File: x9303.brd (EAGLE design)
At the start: 133 x 59 mm, 158 parts, among them CN11 ERC12864-2, CN12 SD-CARD_10P, IC1 7805DT, IC2 L1117, IC3 Pololu, IC4 MCP1700T30, J3 ERASE, K1 TP-1, K2 TP-1, K3 TP-1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

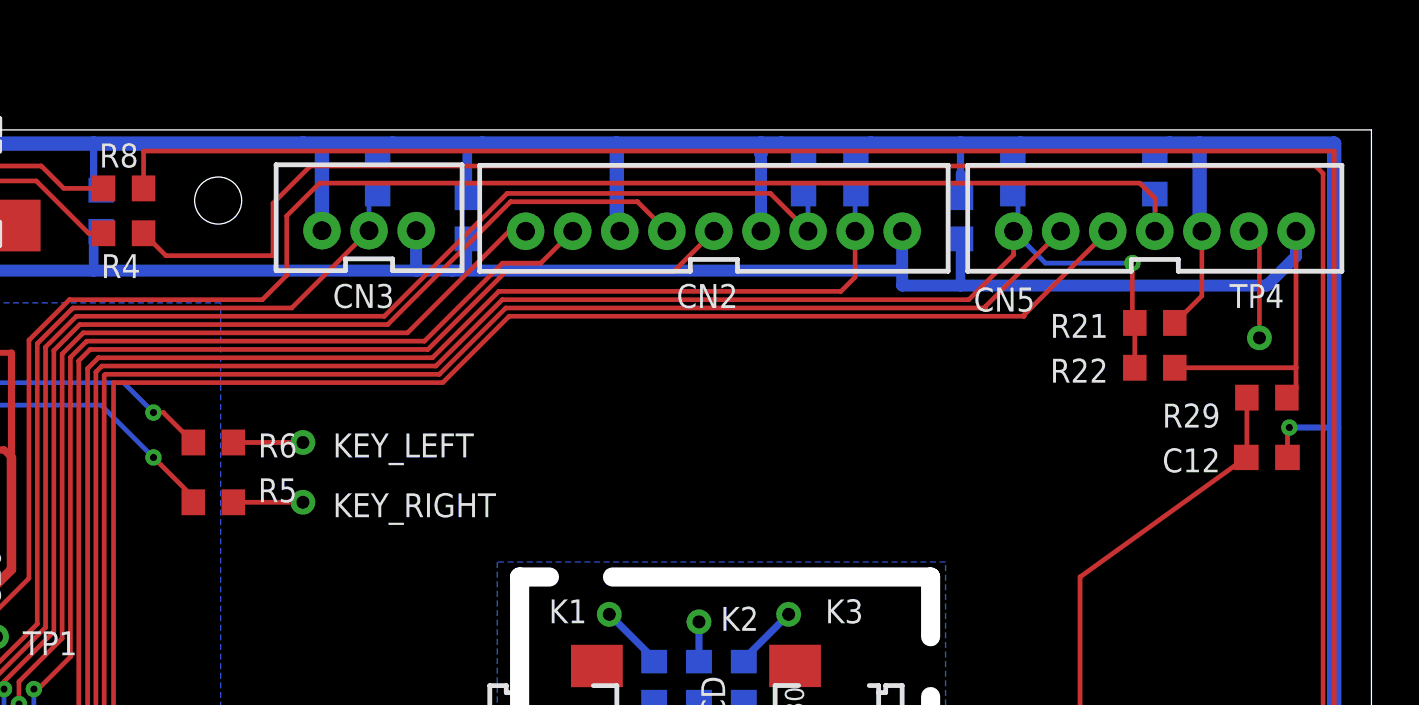
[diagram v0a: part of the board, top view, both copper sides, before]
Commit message: 
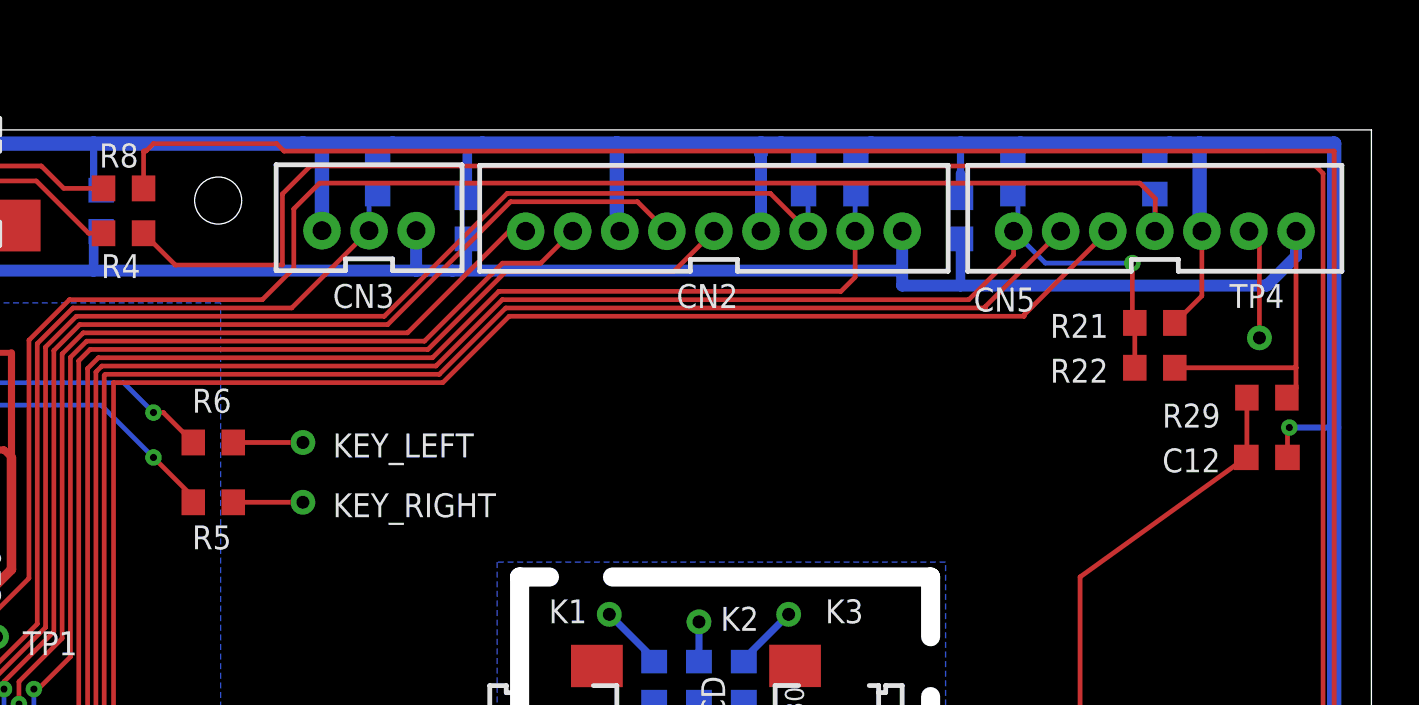
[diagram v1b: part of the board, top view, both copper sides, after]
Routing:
- net KEY-DOWN: track 84.0 -> 84.8 mm
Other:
- board text added: "CHARGER+"
- board text added: "TRN1"
- board text added: "TRN2"
- board text added: "TRN3"
- board text removed: "Chargder+"

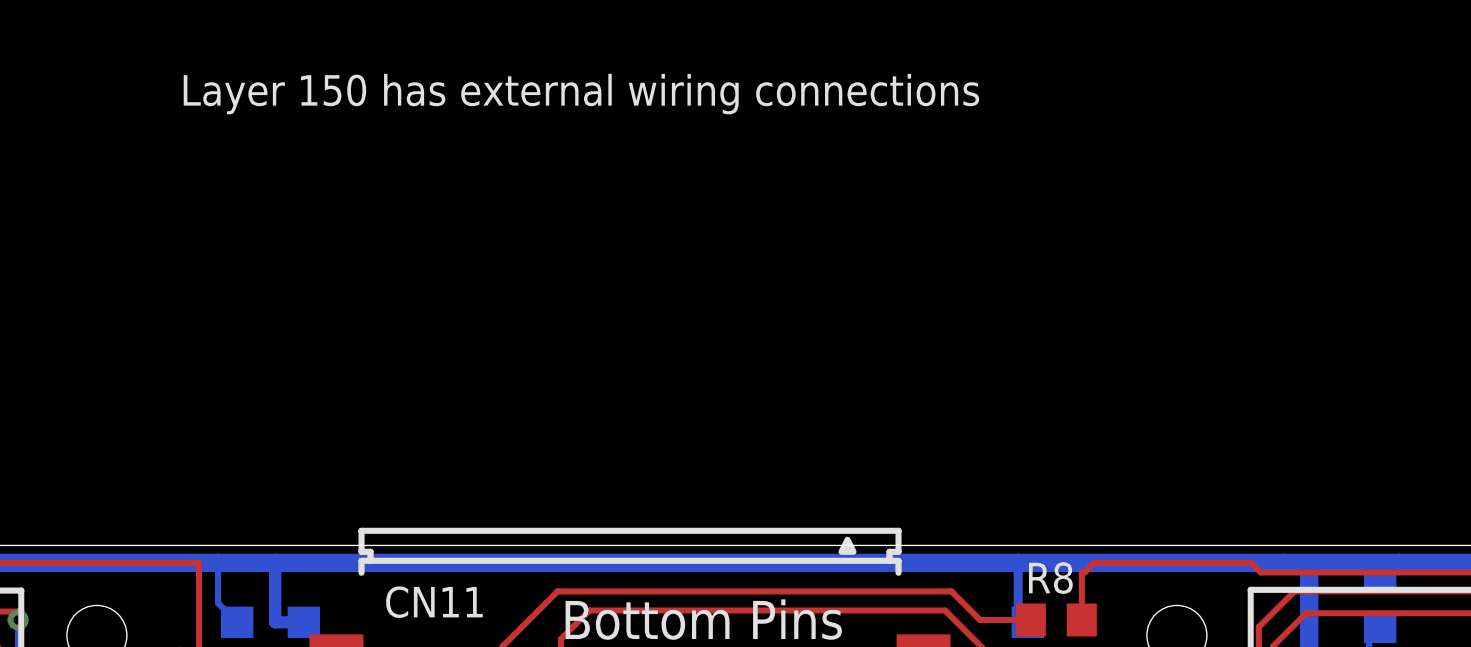
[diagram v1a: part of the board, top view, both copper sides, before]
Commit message: added pictures and docs added firmware binary added old JR9303 wiring and pin-out doc added lcd display adapter patch boards for different displays
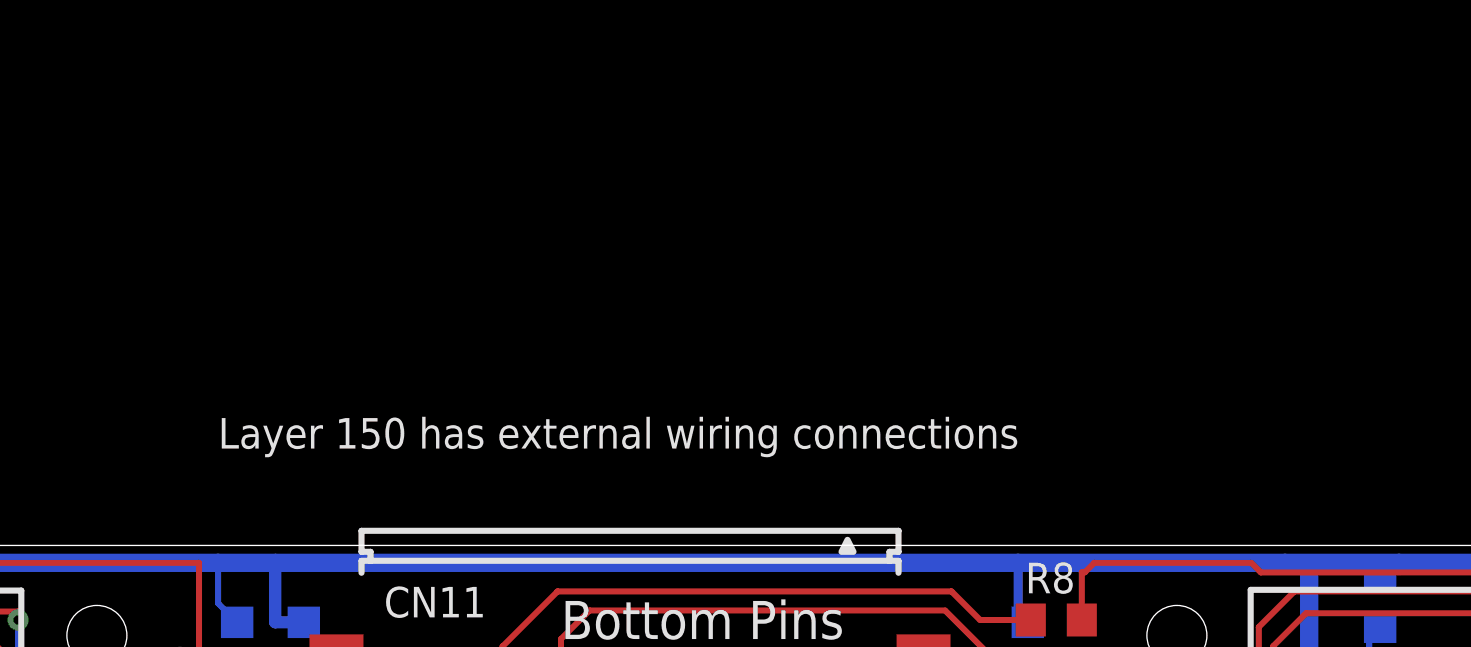
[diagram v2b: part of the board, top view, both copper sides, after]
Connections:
- net PWR_SW_BAT renamed PWR_SW_CTR_A&B
- net RF_MODULE_PWR renamed PWRSW_ON_A
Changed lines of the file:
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@@
 <layer number="14" name="Route14" color="22" fill="1" visible="no" active="no"/>
 <layer number="15" name="Route15" color="23" fill="1" visible="no" active="no"/>
-<layer number="16" name="Bottom" color="1" fill="1" visible="no" active="yes"/>
+<layer number="16" name="Bottom" color="1" fill="1" visible="yes" active="yes"/>
 <layer number="17" name="Pads" color="2" fill="1" visible="yes" active="yes"/>
 <layer number="18" name="Vias" color="2" fill="1" visible="yes" active="yes"/>
@@
 <layer number="20" name="Dimension" color="24" fill="1" visible="yes" active="yes"/>
 <layer number="21" name="tPlace" color="7" fill="1" visible="yes" active="yes"/>
-<layer number="22" name="bPlace" color="7" fill="1" visible="no" active="yes"/>
+<layer number="22" name="bPlace" color="7" fill="1" visible="yes" active="yes"/>
 <layer number="23" name="tOrigins" color="15" fill="1" visible="yes" active="yes"/>
-<layer number="24" name="bOrigins" color="15" fill="1" visible="no" active="yes"/>
+<layer number="24" name="bOrigins" color="15" fill="1" visible="yes" active="yes"/>
 <layer number="25" name="tNames" color="7" fill="1" visible="yes" active="yes"/>
-<layer number="26" name="bNames" color="7" fill="1" visible="no" active="yes"/>
+<layer number="26" name="bNames" color="7" fill="1" visible="yes" active="yes"/>
 <layer number="27" name="tValues" color="7" fill="1" visible="no" active="yes"/>
 <layer number="28" name="bValues" color="7" fill="1" visible="no" active="yes"/>
@@
 <layer number="38" name="bTest" color="7" fill="1" visible="no" active="yes"/>
 <layer number="39" name="tKeepout" color="4" fill="11" visible="yes" active="yes"/>
-<layer number="40" name="bKeepout" color="1" fill="11" visible="no" active="yes"/>
+<layer number="40" name="bKeepout" color="1" fill="11" visible="yes" active="yes"/>
 <layer number="41" name="tRestrict" color="4" fill="10" visible="yes" active="yes"/>
-<layer number="42" name="bRestrict" color="1" fill="10" visible="no" active="yes"/>
+<layer number="42" name="bRestrict" color="1" fill="10" visible="yes" active="yes"/>
 <layer number="43" name="vRestrict" color="2" fill="10" visible="no" active="yes"/>
 <layer number="44" name="Drills" color="7" fill="1" visible="no" active="yes"/>
@@
 <layer number="50" name="dxf" color="7" fill="1" visible="no" active="no"/>
 <layer number="51" name="tDocu" color="7" fill="1" visible="yes" active="yes"/>
-<layer number="52" name="bDocu" color="7" fill="1" visible="no" active="yes"/>
+<layer number="52" name="bDocu" color="7" fill="1" visible="yes" active="yes"/>
 <layer number="53" name="tGND_GNDA" color="7" fill="9" visible="no" active="no"/>
 <layer number="54" name="bGND_GNDA" color="1" fill="9" visible="no" active="no"/>
@@
 <layer number="132" name="bAdjust" color="7" fill="1" visible="no" active="yes"/>
 <layer number="144" name="Drill_legend" color="7" fill="1" visible="no" active="yes"/>
-<layer number="150" name="Notes" color="7" fill="1" visible="no" active="yes"/>
+<layer number="150" name="Notes" color="7" fill="1" visible="yes" active="yes"/>
 <layer number="151" name="HeatSink" color="7" fill="1" visible="no" active="yes"/>
 <layer number="152" name="_bDocu" color="7" fill="1" visible="no" active="yes"/>
@@
 <text x="13.5" y="5.5" size="1.016" layer="150" rot="R180">ROT_PUSH</text>
 <text x="13.5" y="11.5" size="1.016" layer="150" rot="R180">GND</text>
-<text x="64.77" y="73.66" size="1.016" layer="25">Layer 150 has external wiring connections </text>
+<text x="66.04" y="62.23" size="1.016" layer="25">Layer 150 has external wiring connections </text>
 <text x="13.5" y="39" size="1.016" layer="150" rot="R180">TRN3</text>
 <text x="13.5" y="37" size="1.016" layer="150" rot="R180">TRN2</text>
@@
 <contactref element="CN9" pad="1"/>
 </signal>
-<signal name="PWR_SW_BAT">
+<signal name="PWR_SW_CTR_A&amp;B">
 <contactref element="CN9" pad="4"/>
 <contactref element="D3" pad="C"/>
@@
 <wire x1="78.4" y1="10.7725" x2="78.4" y2="9" width="0.2" layer="1"/>
 </signal>
-<signal name="RF_MODULE_PWR">
+<signal name="PWRSW_ON_A">
 <contactref element="CN9" pad="3"/>
 <contactref element="CN8" pad="5"/>
